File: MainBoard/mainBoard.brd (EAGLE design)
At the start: 99 x 99.2 mm, 121 parts, among them IC1 74HC151D, IC2 LM317, IC3 74HC238, J1 22-05-7038-03, J10 22-05-7038-03, J11 22-05-7038-03, J12 22-05-7038-03, J13 22-05-7038-03, J14 22-05-7038-03, J15 22-05-7038-03, J16 22-05-7038-03, J2 22-05-7038-03, J3 22-05-7038-03, J4 22-05-7038-03, J5 22-05-7038-03, J6 22-05-7038-03, J7 22-05-7038-03, J8 22-05-7038-03, J9 22-05-7038-03, Q1 8MHz, Q10 BC847ASMD, Q12 BC847ASMD, Q2 BC847ASMD, Q4 BC847ASMD, Q6 BC847ASMD, Q8 BC847ASMD, X1 PWR12, X10 MSTBA2, X11 MSTBA2, X12 MSTBA2, X13 MSTBA2, X2 MSTBA2, X3 MSTBA2, X4 MSTBA2, X5 MSTBA2, X6 MSTBA2, X7 MSTBA2, X8 MSTBA2, X9 MSTBA2

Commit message: mainboard updates...
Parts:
- U$1: value STM32F051 -> STM32 F051 R4T6

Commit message: mainboard updates
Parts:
- added C18: 4.7u/35V, rcl:PANASONIC_B
- added C19: 10n, rcl:C0603K
- added C2, C20: 100n, rcl:C0603K
- added IC4: FT232RL, ftdichip:SSOP28
- added J19: J7MM, jumper:07
- added R37, R38: EMI 60Ohm Ferrit, rcl:R0603
- added SJ1: (no value), jumper:SJ
- added X15: MINI-USB-SCHIELD-32005-301, con-cypressindustries:32005-301
- moved SV1 83.6 mm to (6.60, 45.0), turned to 0 degrees
- moved R36 77.9 mm to (6.60, 49.0), turned to 180 degrees
- moved R31 11.7 mm to (76.7, 75.4), turned to 90 degrees
- moved R30 8.18 mm to (74.2, 75.4), turned to 90 degrees
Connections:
- new net DM: IC4.16, X15.2
- new net DP: IC4.15, X15.3
- new net ID: X15.4
- new net N$27: R38.2, SJ1.2, X15.M3
- new net N$32: C20.1, IC4.17
- new net PB0: R17.1, U$1.26
- new net PB10: R21.1, U$1.29
- new net VBUS: C19.1, R37.1, X15.1
- new net VCCUSB: C18.+, C2.1, IC4.20, IC4.4, R37.2
- net +3V3: now also J19.1, J19.2, S2.2, S3.2, S4.2
- net GND: now also C18.-, C19.2, C2.2, C20.2, IC4.18, IC4.21, IC4.25, IC4.7, R38.1, SJ1.1, X15.5
- net PA4: now also R2.1; no longer R13.1
- net PA5: no longer R17.1
- net PA6: now also R9.1; no longer R21.1
- net PA7: now also R13.1; no longer R26.1
- net PA8: now also R26.1
- net PF4: no longer R2.1
- net PF5: no longer R9.1
- net USART1_RX: now also IC4.1
- net USART1_TX: now also IC4.5
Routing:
- net +3V3: track 53.1 -> 271.0 mm, vias 3 -> 6
- net PA8: track 0.00 -> 56.7 mm
- net PB10: track 0.00 -> 39.6 mm
- net USART2_TX: track 0.00 -> 38.9 mm, vias 0 -> 1
- net PF4: track 38.6 -> 0.00 mm
- net USART2_RX: track 68.6 -> 33.9 mm
- net WIFI_RESET: track 5.47 -> 37.7 mm, vias 0 -> 1
- net PA5: track 31.3 -> 0.00 mm
- net PB0: track 0.00 -> 29.8 mm
- net PF5: track 29.1 -> 0.00 mm
- net PA7: track 51.6 -> 28.8 mm
- net PA4: track 27.3 -> 48.7 mm
- net VCCUSB: track 0.00 -> 21.1 mm, vias 0 -> 1
- net DM: track 0.00 -> 18.2 mm
- net VBUS: track 0.00 -> 13.2 mm, vias 0 -> 1
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- added copper zone on layer 16, net N$28

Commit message: mainboard updates
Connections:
- net GND renamed GND123
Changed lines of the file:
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@@
 <contactref element="U$1" pad="1"/>
 </signal>
-<signal name="GND">
+<signal name="GND123">
 <contactref element="C9" pad="2"/>
 <contactref element="C11" pad="-"/>

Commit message: mainboard updates
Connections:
- removed net D_SCLK_SCL: SV5.5
- removed net D_SID_SDAIN: SV5.6
- removed net D_SOD_SDAOUT: SV5.7
- removed net PB3: U$1.55
- removed net PF4: U$1.18
- removed net PF5: U$1.19
- new net SPI1_MISO: SV5.7, U$1.56
- new net SPI1_MOSI: SV5.6, U$1.57
- new net SPI1_SCK: SV5.5, U$1.55
- net D_IM1: now also U$1.18
- net D_IM2: now also U$1.19
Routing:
- net D_IM2: track 0.00 -> 18.4 mm
- net D_IM1: track 0.00 -> 17.6 mm
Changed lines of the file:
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@@
 <via x="38.608" y="67.31" extent="1-16" drill="0.6"/>
 <via x="25.146" y="84.582" extent="1-16" drill="0.6"/>
-<via x="40.386" y="71.882" extent="1-16" drill="0.6"/>
+<via x="39.624" y="73.914" extent="1-16" drill="0.6"/>
 <contactref element="IC4" pad="7"/>
 <contactref element="IC4" pad="21"/>
@@
 <wire x1="54.82510625" y1="31.53489375" x2="49.56889375" y2="36.79110625" width="0.6096" layer="1"/>
 <wire x1="49.56889375" y1="36.79110625" x2="49.276" y2="37.4982125" width="0.6096" layer="1" curve="-45"/>
-<wire x1="49.276" y1="37.4982125" x2="49.276" y2="46.5757875" width="0.6096" layer="1"/>
-<wire x1="49.276" y1="46.5757875" x2="48.98310625" y2="47.28289375" width="0.6096" layer="1" curve="45"/>
-<wire x1="48.98310625" y1="47.28289375" x2="45.974" y2="50.292" width="0.6096" layer="1"/>
-<wire x1="45.974" y1="50.292" x2="45.974" y2="59.076790625" width="0.3048" layer="1"/>
+<wire x1="49.276" y1="37.4982125" x2="49.276" y2="44.0357875" width="0.6096" layer="1"/>
+<wire x1="49.276" y1="44.45" x2="45.974" y2="47.752" width="0.3048" layer="1"/>
+<wire x1="45.974" y1="47.752" x2="45.974" y2="59.076790625" width="0.3048" layer="1"/>
 <wire x1="45.974" y1="59.076790625" x2="46.228" y2="59.69" width="0.3048" layer="1" curve="-45"/>
 <wire x1="46.228" y1="59.69" x2="46.23765625" y2="59.686" width="0.3048" layer="1" curve="45"/>
 <wire x1="46.23765625" y1="59.686" x2="47.252" y2="59.686" width="0.3048" layer="1"/>
+<wire x1="49.276" y1="44.0357875" x2="49.276" y2="44.45" width="0.3048" layer="1"/>
 </signal>
 <signal name="NRST">
@@
 <contactref element="U$1" pad="43"/>
 </signal>
-<signal name="PB3">
+<signal name="SPI1_SCK">
 <contactref element="U$1" pad="55"/>
+<contactref element="SV5" pad="5"/>
+<wire x1="66.04" y1="36.068" x2="42.152" y2="65.236" width="0" layer="19" extent="1-1"/>
 </signal>
 <signal name="N$1">
@@
 <wire x1="63.5" y1="10.16" x2="63.5" y2="3.048" width="1.778" layer="16"/>
 </signal>
-<signal name="PF4">
-<contactref element="U$1" pad="18"/>
-</signal>
-<signal name="PF5">
-<contactref element="U$1" pad="19"/>
-</signal>
 <signal name="PA4">
 <contactref element="U$1" pad="20"/>
@@
 <wire x1="42.63310625" y1="34.75910625" x2="42.926" y2="35.4662125" width="0.6096" layer="1" curve="45"/>
 <wire x1="42.926" y1="35.4662125" x2="42.926" y2="44.0357875" width="0.6096" layer="1"/>
-<wire x1="42.926" y1="44.0357875" x2="42.63310625" y2="44.74289375" width="0.6096" layer="1" curve="45"/>
-<wire x1="42.63310625" y1="44.74289375" x2="39.116" y2="48.26" width="0.6096" layer="1"/>
-<wire x1="39.116" y1="48.26" x2="39.152" y2="48.3469125" width="0.3048" layer="1" curve="45"/>
-<wire x1="39.152" y1="48.3469125" x2="39.152" y2="53.636" width="0.3048" layer="1"/>
+<wire x1="42.926" y1="45.72" x2="39.152" y2="49.494" width="0.3048" layer="1"/>
+<wire x1="39.152" y1="49.494" x2="39.152" y2="53.636" width="0.3048" layer="1"/>
+<wire x1="42.926" y1="44.0357875" x2="42.926" y2="45.72" width="0.3048" layer="1"/>
 </signal>
 <signal name="PA5">
@@
 <wire x1="41.94889375" y1="32.29689375" x2="43.90310625" y2="34.25110625" width="0.6096" layer="1"/>
 <wire x1="43.90310625" y1="34.25110625" x2="44.196" y2="34.9582125" width="0.6096" layer="1" curve="45"/>
-<wire x1="44.196" y1="34.9582125" x2="44.196" y2="44.5437875" width="0.6096" layer="1"/>
-<wire x1="44.196" y1="44.5437875" x2="43.90310625" y2="45.25089375" width="0.6096" layer="1" curve="45"/>
-<wire x1="43.90310625" y1="45.25089375" x2="40.132" y2="49.022" width="0.6096" layer="1"/>
-<wire x1="40.132" y1="49.022" x2="40.152" y2="49.070284375" width="0.3048" layer="1" curve="45"/>
-<wire x1="40.152" y1="49.070284375" x2="40.152" y2="53.636" width="0.3048" layer="1"/>
+<wire x1="44.196" y1="34.9582125" x2="44.196" y2="44.0357875" width="0.6096" layer="1"/>
+<wire x1="40.152" y1="49.51" x2="40.152" y2="53.636" width="0.3048" layer="1"/>
+<wire x1="44.196" y1="45.466" x2="40.152" y2="49.51" width="0.3048" layer="1"/>
+<wire x1="44.196" y1="44.0357875" x2="44.196" y2="45.466" width="0.3048" layer="1"/>
 </signal>
 <signal name="S1_DAT">
@@
 <wire x1="41.76089375" y1="30.33089375" x2="45.17310625" y2="33.74310625" width="0.6096" layer="1"/>
 <wire x1="45.17310625" y1="33.74310625" x2="45.466" y2="34.4502125" width="0.6096" layer="1" curve="45"/>
-<wire x1="45.466" y1="34.4502125" x2="45.466" y2="45.0517875" width="0.6096" layer="1"/>
-<wire x1="45.466" y1="45.0517875" x2="45.17310625" y2="45.75889375" width="0.6096" layer="1" curve="45"/>
-<wire x1="45.17310625" y1="45.75889375" x2="41.148" y2="49.784" width="0.6096" layer="1"/>
-<wire x1="41.148" y1="49.784" x2="40.94489375" y2="49.98710625" width="0.3048" layer="1"/>
-<wire x1="40.94489375" y1="49.98710625" x2="40.652" y2="50.6942125" width="0.3048" layer="1" curve="-45"/>
-<wire x1="40.652" y1="50.6942125" x2="40.652" y2="53.636" width="0.3048" layer="1"/>
+<wire x1="45.466" y1="34.4502125" x2="45.466" y2="44.0357875" width="0.6096" layer="1"/>
+<wire x1="45.466" y1="45.212" x2="40.652" y2="50.026" width="0.3048" layer="1"/>
+<wire x1="40.652" y1="50.026" x2="40.652" y2="53.636" width="0.3048" layer="1"/>
+<wire x1="45.466" y1="44.0357875" x2="45.466" y2="45.212" width="0.3048" layer="1"/>
 </signal>
 <signal name="WP6">
@@
 <signal name="D_IM2">
 <contactref element="SV4" pad="4"/>
+<contactref element="U$1" pad="19"/>
+<wire x1="40.64" y1="36.068" x2="40.64" y2="46.99" width="0.3048" layer="1"/>
+<wire x1="40.64" y1="46.99" x2="38.652" y2="48.978" width="0.3048" layer="1"/>
+<wire x1="38.652" y1="48.978" x2="38.652" y2="53.636" width="0.3048" layer="1"/>
 </signal>
 <signal name="D_IM1">
 <contactref element="SV4" pad="3"/>
-</signal>
-<signal name="D_SOD_SDAOUT">
-<contactref element="SV5" pad="7"/>
-</signal>
-<signal name="D_SID_SDAIN">
-<contactref element="SV5" pad="6"/>
-</signal>
-<signal name="D_SCLK_SCL">
-<contactref element="SV5" pad="5"/>
+<contactref element="U$1" pad="18"/>
+<wire x1="38.1" y1="36.068" x2="38.152" y2="36.12" width="0.3048" layer="1"/>
+<wire x1="38.152" y1="36.12" x2="38.152" y2="53.636" width="0.3048" layer="1"/>
 </signal>
 <signal name="D_ENABLE">
@@
 <wire x1="52.85910625" y1="29.94489375" x2="47.02889375" y2="35.77510625" width="0.6096" layer="1"/>
 <wire x1="47.02889375" y1="35.77510625" x2="46.736" y2="36.4822125" width="0.6096" layer="1" curve="-45"/>
-<wire x1="46.736" y1="36.4822125" x2="46.736" y2="45.5597875" width="0.6096" layer="1"/>
-<wire x1="46.736" y1="45.5597875" x2="46.44310625" y2="46.26689375" width="0.6096" layer="1" curve="45"/>
-<wire x1="46.44310625" y1="46.26689375" x2="42.164" y2="50.546" width="0.6096" layer="1"/>
-<wire x1="42.164" y1="50.546" x2="42.152" y2="50.574971875" width="0.3048" layer="1" curve="-45"/>
-<wire x1="42.152" y1="50.574971875" x2="42.152" y2="53.636" width="0.3048" layer="1"/>
+<wire x1="46.736" y1="36.4822125" x2="46.736" y2="44.0357875" width="0.6096" layer="1"/>
+<wire x1="46.736" y1="44.958" x2="42.152" y2="49.542" width="0.3048" layer="1"/>
+<wire x1="42.152" y1="49.542" x2="42.152" y2="53.636" width="0.3048" layer="1"/>
+<wire x1="46.736" y1="44.0357875" x2="46.736" y2="44.958" width="0.3048" layer="1"/>
 </signal>
 <signal name="PB10">
@@
 <wire x1="54.31710625" y1="30.26489375" x2="48.29889375" y2="36.28310625" width="0.6096" layer="1"/>
 <wire x1="48.29889375" y1="36.28310625" x2="48.006" y2="36.9902125" width="0.6096" layer="1" curve="-45"/>
-<wire x1="48.006" y1="36.9902125" x2="48.006" y2="46.0677875" width="0.6096" layer="1"/>
-<wire x1="48.006" y1="46.0677875" x2="47.71310625" y2="46.77489375" width="0.6096" layer="1" curve="45"/>
-<wire x1="47.71310625" y1="46.77489375" x2="43.688" y2="50.8" width="0.6096" layer="1"/>
-<wire x1="43.688" y1="50.8" x2="43.652" y2="50.8869125" width="0.3048" layer="1" curve="-45"/>
-<wire x1="43.652" y1="50.8869125" x2="43.652" y2="53.636" width="0.3048" layer="1"/>
+<wire x1="48.006" y1="36.9902125" x2="48.006" y2="44.0357875" width="0.6096" layer="1"/>
+<wire x1="48.006" y1="44.704" x2="43.652" y2="49.058" width="0.3048" layer="1"/>
+<wire x1="43.652" y1="49.058" x2="43.652" y2="53.636" width="0.3048" layer="1"/>
+<wire x1="48.006" y1="44.0357875" x2="48.006" y2="44.704" width="0.3048" layer="1"/>
 </signal>
 <signal name="N$26">
@@
 </polygon>
 </signal>
+<signal name="SPI1_MISO">
+<contactref element="U$1" pad="56"/>
+<contactref element="SV5" pad="7"/>
+<wire x1="41.652" y1="65.236" x2="71.12" y2="36.068" width="0" layer="19" extent="1-1"/>
+</signal>
+<signal name="SPI1_MOSI">
+<contactref element="U$1" pad="57"/>
+<contactref element="SV5" pad="6"/>
+<wire x1="68.58" y1="36.068" x2="41.152" y2="65.236" width="0" layer="19" extent="1-1"/>
+</signal>
 </signals>

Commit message: mainboard updates
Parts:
- added LED2: (no value), led:LED3MM
- added R39: 100, rcl:R0805
- J19: value J7MM -> J5MM; device jumper:07 -> jumper:05
- moved C3 1.93 mm to (44.7, 58.4), turned to 90 degrees
- moved J19 0.76 mm to (46.0, 85.9)
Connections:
- removed net GND123: C1.-, C10.2, C11.-, C18.-, C19.2, C2.2, C20.2, C3.2, C4.2, C5.2, C6.2, C7.2, C8.2, C9.2, D1.A, D2.A, D3.A, D4.A, D5.A, D6.A, IC1.8, IC3.8, IC4.18, IC4.21, IC4.25, IC4.7, J1.3, J10.3, J11.3, J12.3, J13.3, J14.3, J15.3, J16.3, J2.3, J3.3, J4.3, J5.3, J6.3, J7.3, J8.3, J9.3, JP1.3, JP3.4, Q10.2, Q12.2, Q2.2, Q4.2, Q6.2, Q8.2, R1.1, R10.1, R14.1, R18.1, R22.1, R27.1, R3.2, R32.1, R33.1, R34.1, R35.1, R36.1, R38.1, R4.1, SJ1.1, SV1.7, SV3.1, SV3.2, SV3.3, SV4.1, U$1.12, U$1.31, U$1.60, U$1.63, X1.2, X10.2, X11.2, X12.2, X13.2, X15.5, X2.2, X3.2, X4.2, X5.2, X6.2, X7.2, X8.2, X9.2
- new net ERROR_LED: LED2.A, U$1.2
- new net GND: C1.-, C10.2, C11.-, C18.-, C19.2, C2.2, C20.2, C3.2, C4.2, C5.2, C6.2, C7.2, C8.2, C9.2, D1.A, D2.A, D3.A, D4.A, D5.A, D6.A, IC1.8, IC3.8, IC4.18, IC4.21, IC4.25, IC4.7, J1.3, J10.3, J11.3, J12.3, J13.3, J14.3, J15.3, J16.3, J2.3, J3.3, J4.3, J5.3, J6.3, J7.3, J8.3, J9.3, JP1.3, JP3.4, Q10.2, Q12.2, Q2.2, Q4.2, Q6.2, Q8.2, R1.1, R10.1, R14.1, R18.1, R22.1, R27.1, R3.2, R32.1, R33.1, R34.1, R35.1, R36.1, R38.1, R39.1, R4.1, SJ1.1, SV1.7, SV3.1, SV3.2, SV3.3, SV4.1, U$1.12, U$1.31, U$1.60, U$1.63, X1.2, X10.2, X11.2, X12.2, X13.2, X15.5, X2.2, X3.2, X4.2, X5.2, X6.2, X7.2, X8.2, X9.2
- new net N$29: LED2.K, R39.2
- net D_ENABLE: now also U$1.40
- net D_RESET: now also U$1.37
- net D_RS: now also U$1.38
- net D_RW: now also U$1.39
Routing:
- net SPI1_MOSI: track 0.00 -> 55.2 mm, vias 0 -> 2
- net SPI1_MISO: track 0.00 -> 54.1 mm, vias 0 -> 1
- net SPI1_SCK: track 0.00 -> 42.2 mm, vias 0 -> 1
- net D_ENABLE: track 0.00 -> 36.8 mm, vias 0 -> 2
- net D_RW: track 0.00 -> 33.5 mm, vias 0 -> 2
- net D_RS: track 0.00 -> 30.6 mm, vias 0 -> 2
- net D_RESET: track 0.00 -> 27.8 mm, vias 0 -> 2
- net ERROR_LED: track 0.00 -> 25.0 mm, vias 0 -> 1
- net GND: track 0.00 -> 17.6 mm, vias 0 -> 48
- net GND123: track 17.4 -> 0.00 mm, vias 33 -> 0
- net FREQ: track 27.3 -> 30.0 mm
- net N$29: track 0.00 -> 2.61 mm
- net SWDIO: track 35.6 -> 35.1 mm
- added copper zone on layer 1, net GND
- added copper zone on layer 16, net GND
- removed copper zone on layer 1, net GND123
- removed copper zone on layer 16, net GND123
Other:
- board text added: "ERR"
- board text added: "WaterCtrl v0.1"
- board text added: "github.com/janhieber/WaterCtrl"
- board text removed: "ESP8266"

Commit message: moisture and main board updates
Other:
- outline, holes or cut-outs redrawn
- board text added: "- +"
- board text added: "1"
- board text added: "2"
- board text added: "3"
- board text added: "3V3"
- board text added: "4"
- board text added: "7"
- board text added: "8"
- board text added: "BT1 BT2 BT3 BT4"
- board text added: "CLK"
- board text added: "ESP8266"
- board text added: "EXT PWR"
- board text added: "GND"
- board text added: "GND 12VDC"
- board text added: "GND TX RX NC"
- board text added: "GND [+]"
- board text added: "IO"
- board text added: "M1"
- board text added: "M2"
- board text added: "M3"
- board text added: "M4"
- board text added: "M5"
- board text added: "M6"
- board text added: "NC"
- board text added: "NRST"
- board text added: "S1"
- board text added: "S2"
- board text added: "S3"
- board text added: "S4"
- board text added: "S5"
- board text added: "S6"
- board text added: "S7"
- board text added: "S8"
- board text added: "SEN"
- board text added: "SWD"
- board text added: "UART"
- board text added: "VREG"

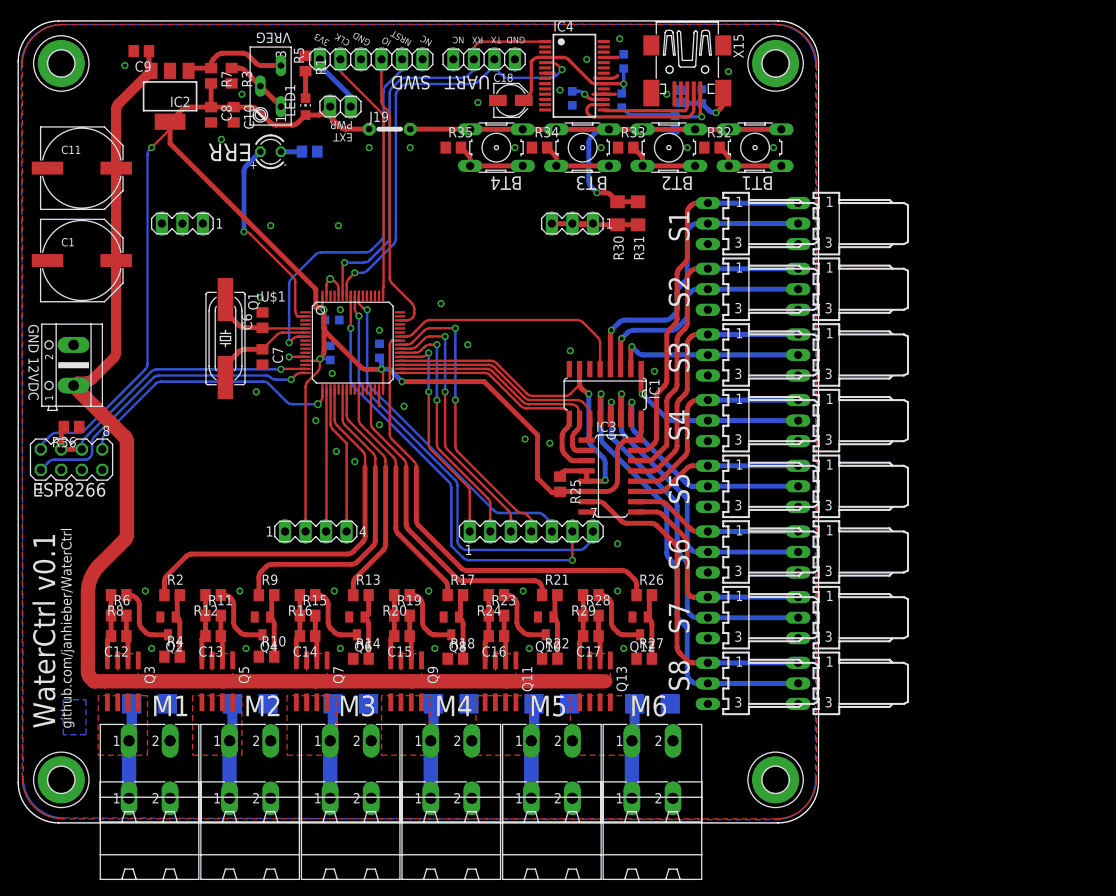
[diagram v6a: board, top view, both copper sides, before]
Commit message: mainboard silkscreen tuning
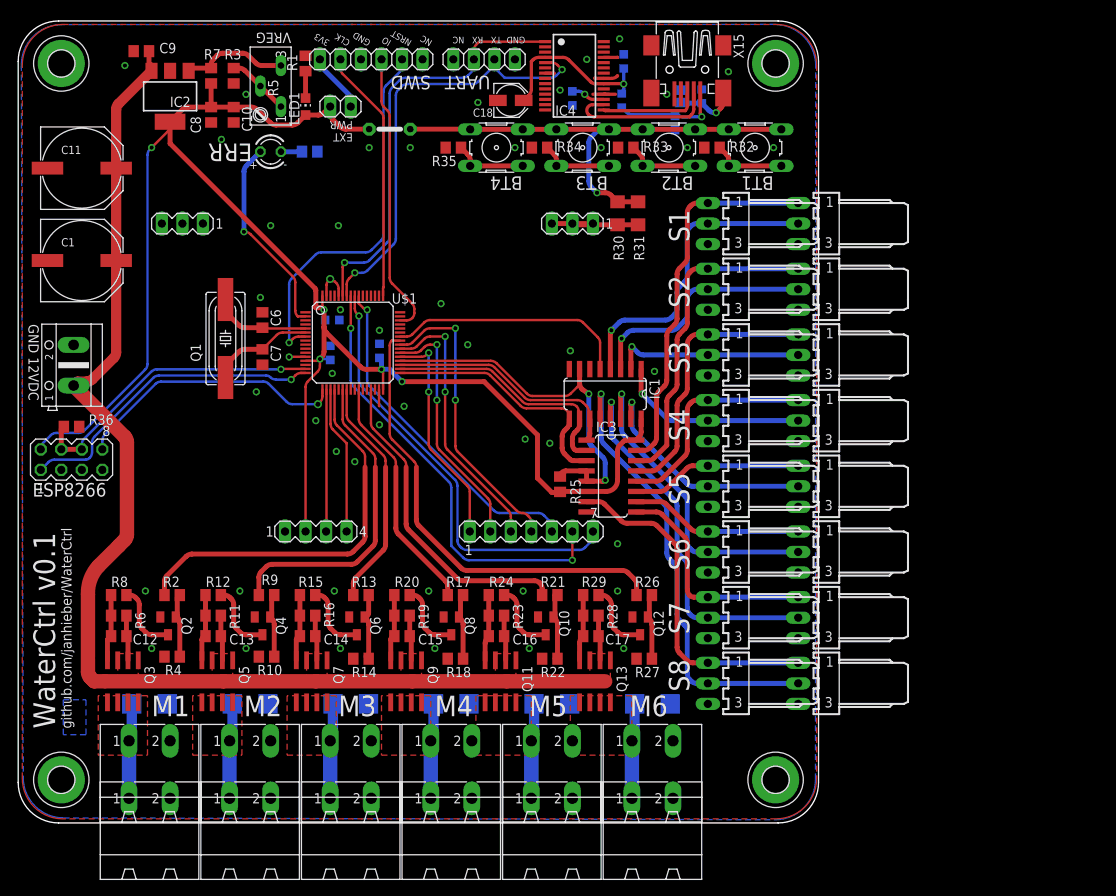
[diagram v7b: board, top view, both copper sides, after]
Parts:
- moved R3 0.25 mm to (26.7, 92.5)

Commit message: fix BOM generation; some board fixes
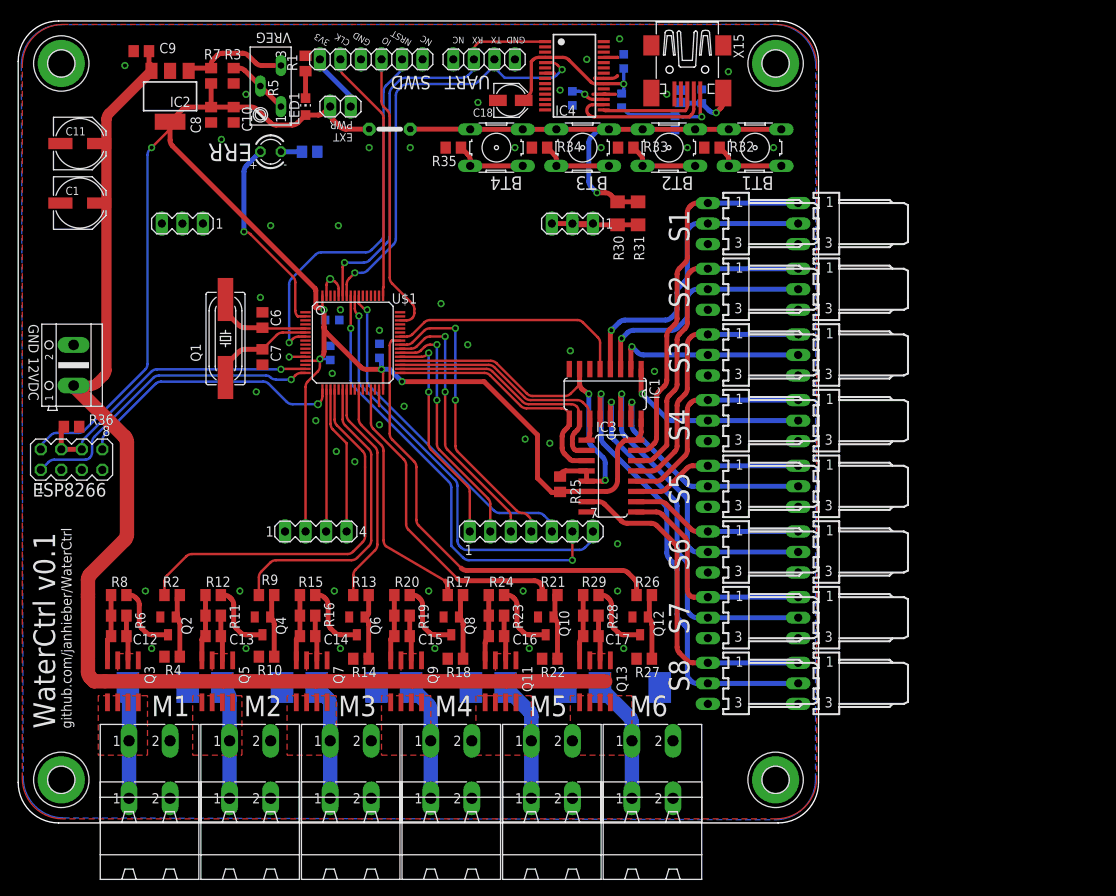
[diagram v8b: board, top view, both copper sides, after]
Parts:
- added U$10, U$3, U$4, U$5, U$6, U$7, U$8, U$9: PSK 254/3W, extra:DUMMY_BOM
- added U$11: EA DOGM204W-A, extra:DUMMY_BOM
- added U$12, U$13, U$14, U$15, U$16, U$17: AKL 249-02, extra:DUMMY_BOM
- added U$18, U$19: Kontakte (20Stk), extra:DUMMY_BOM
- C1, C11: device rcl:PANASONIC_G -> rcl:PANASONIC_D
- D1, D2, D3, D4, D5, D6: device diode:SMB -> diode:SMC
- moved C1 7.12 mm to (7.62, 76.7)
- moved D6 3.45 mm to (75.7, 16.8)
- moved C11 3.06 mm to (7.62, 84.1)
- moved D5 2.87 mm to (64.0, 16.8)
- moved D4 2.40 mm to (52.3, 16.8)
- moved D1 2.27 mm to (17.3, 16.8)
- moved D3 2.09 mm to (40.6, 16.8)
- moved D2 2.05 mm to (29.0, 16.8)
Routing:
- net WP6: track 11.8 -> 15.3 mm
- net WP5: track 11.8 -> 15.0 mm
- net WP4: track 11.8 -> 14.7 mm
- net WP3: track 11.8 -> 14.3 mm
- net WP2: track 11.8 -> 14.0 mm
- net WP1: track 11.8 -> 13.7 mm
- net PB0: track 29.7 -> 30.9 mm
- net PA7: track 28.8 -> 28.0 mm
- net +12V: track 181.1 -> 181.9 mm
- net PA6: track 39.0 -> 38.3 mm
- removed copper zone on layer 16, net N$28
